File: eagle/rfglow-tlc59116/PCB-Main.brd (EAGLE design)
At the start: 20.1 x 75.9 mm, 14 parts, among them IC1 TLC59116PW, J1 4P-SMD-2.0-90D, J2 2P-2.0-90D-SMD, SW1 MK-12C02 G1.5, SW2 DHT-4235A, X1 87438-06

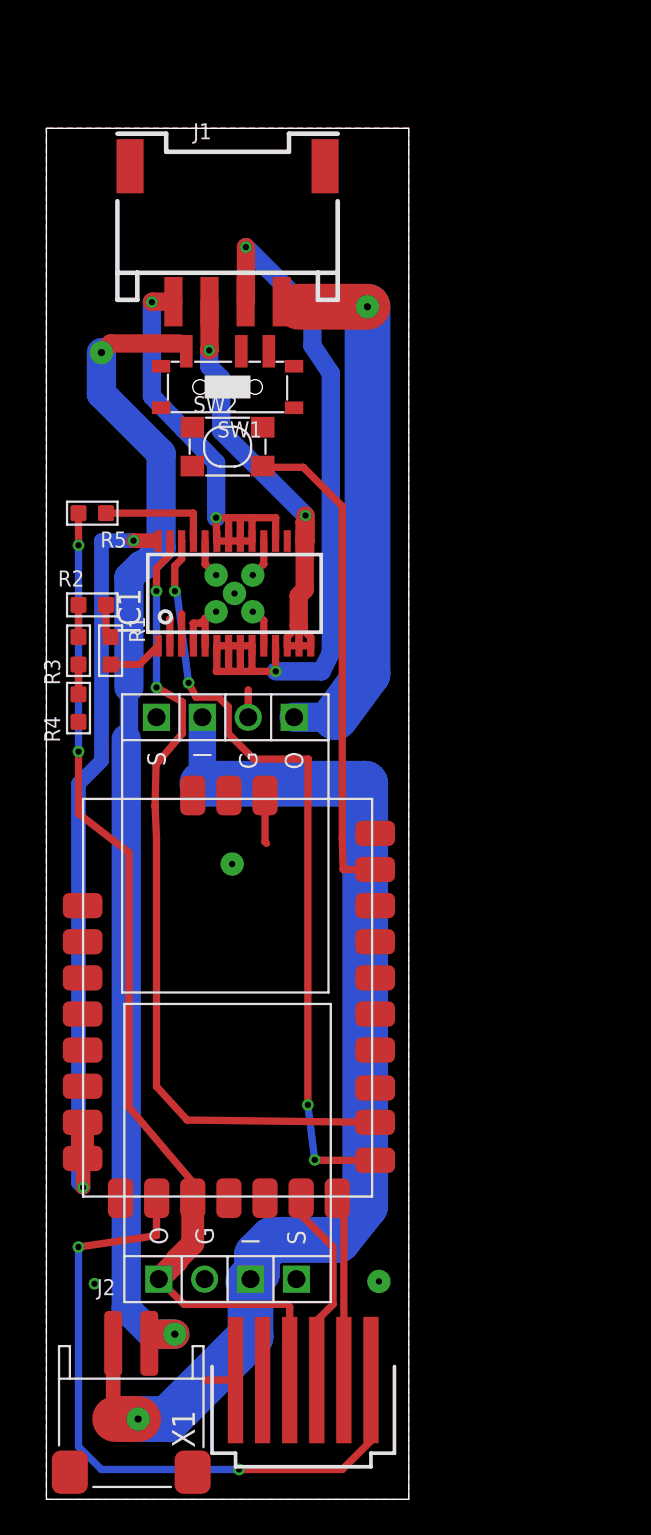
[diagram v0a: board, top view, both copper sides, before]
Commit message: CLeaned up gerbers, fixed serious circuit errors
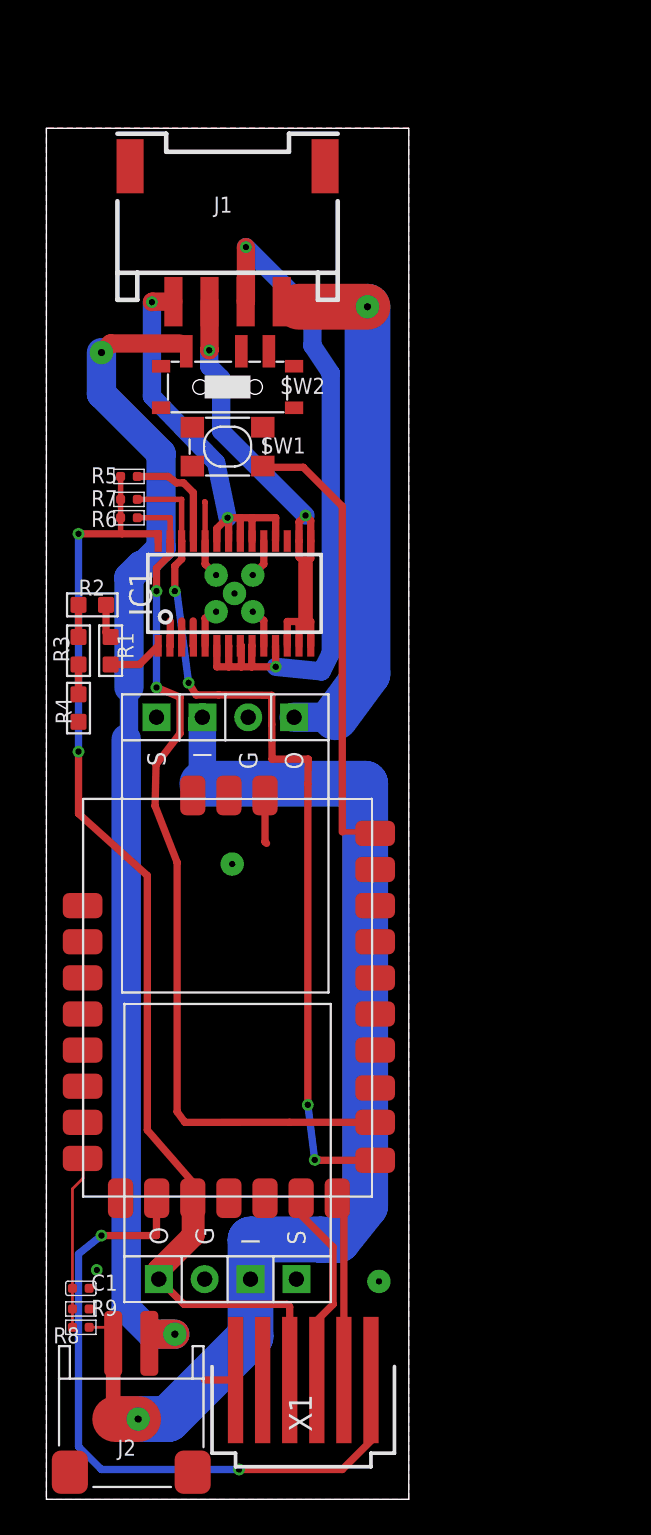
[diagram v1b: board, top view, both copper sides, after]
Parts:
- added C1: 100nf, Seeed-Capacitor:C0402
- added R6, R7: 4.7K, Seeed-Resistor:R0402
- added R8, R9: 10M 1/16W, Seeed-Resistor:R0402
- R5: value 10K -> 10K 1/16W; device Seeed-Resistor:R0603 -> Seeed-Resistor:R0402
- X1: device con-molex:87438-06 -> Components:87438-06
- moved R5 2.87 mm to (-6.86, 51.6)
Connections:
- removed net N$12: IC1.26, U$1.P$18
- removed net N$13: IC1.27, U$1.P$19
- removed net N$8: MOD3.3V.O, R5.1, U$1.P$13, X1.3
- new net I2CSCL: IC1.26, R7.1, U$1.P$18
- new net I2CSDA: IC1.27, R6.1, U$1.P$19
- new net V3.3: IC1.28, MOD3.3V.O, R5.1, R6.2, R7.2, U$1.P$13, X1.3
- net GND: now also C1.1, R9.1
- net N$11: now also U$1.P$27; no longer U$1.P$26
- net N$17: now also C1.2, R8.1, R9.2; no longer IC1.28, U$1.P$9
- net N$5: now also R8.2
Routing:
- net V3.3: track 0.00 -> 64.8 mm, vias 0 -> 2
- net N$8: track 57.8 -> 0.00 mm, vias 2 -> 0
- net I2CSCL: track 0.00 -> 48.9 mm, vias 0 -> 4
- net I2CSDA: track 0.00 -> 48.2 mm, vias 0 -> 2
- net N$13: track 44.8 -> 0.00 mm, vias 2 -> 0
- net N$12: track 43.1 -> 0.00 mm, vias 4 -> 0
- net N$17: track 43.2 -> 9.60 mm, vias 2 -> 0
- net N$14: track 43.4 -> 40.2 mm
- net N$5: track 62.4 -> 65.2 mm
- net N$15: track 26.3 -> 24.0 mm
- net N$11: track 27.2 -> 25.3 mm
- net GND: track 20.6 -> 19.4 mm
- net N$10: track 29.9 -> 29.1 mm

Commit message: Updates to board
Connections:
- new net N$8: U$1.P$11, X1.2
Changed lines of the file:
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@@
 <?xml version="1.0" encoding="utf-8"?>
 <!DOCTYPE eagle SYSTEM "eagle.dtd">
-<eagle version="8.3.0">
+<eagle version="8.3.1">
 <drawing>
 <settings>
@@
 <wire x1="-9.398" y1="13.769" x2="-9.424" y2="13.795" width="0.1524" layer="1"/>
 </signal>
+<signal name="N$8">
+<contactref element="U$1" pad="P$11"/>
+<contactref element="X1" pad="2"/>
+<wire x1="0.544" y1="1.524" x2="-7.324" y2="11.595" width="0" layer="19" extent="1-1"/>
+</signal>
 </signals>

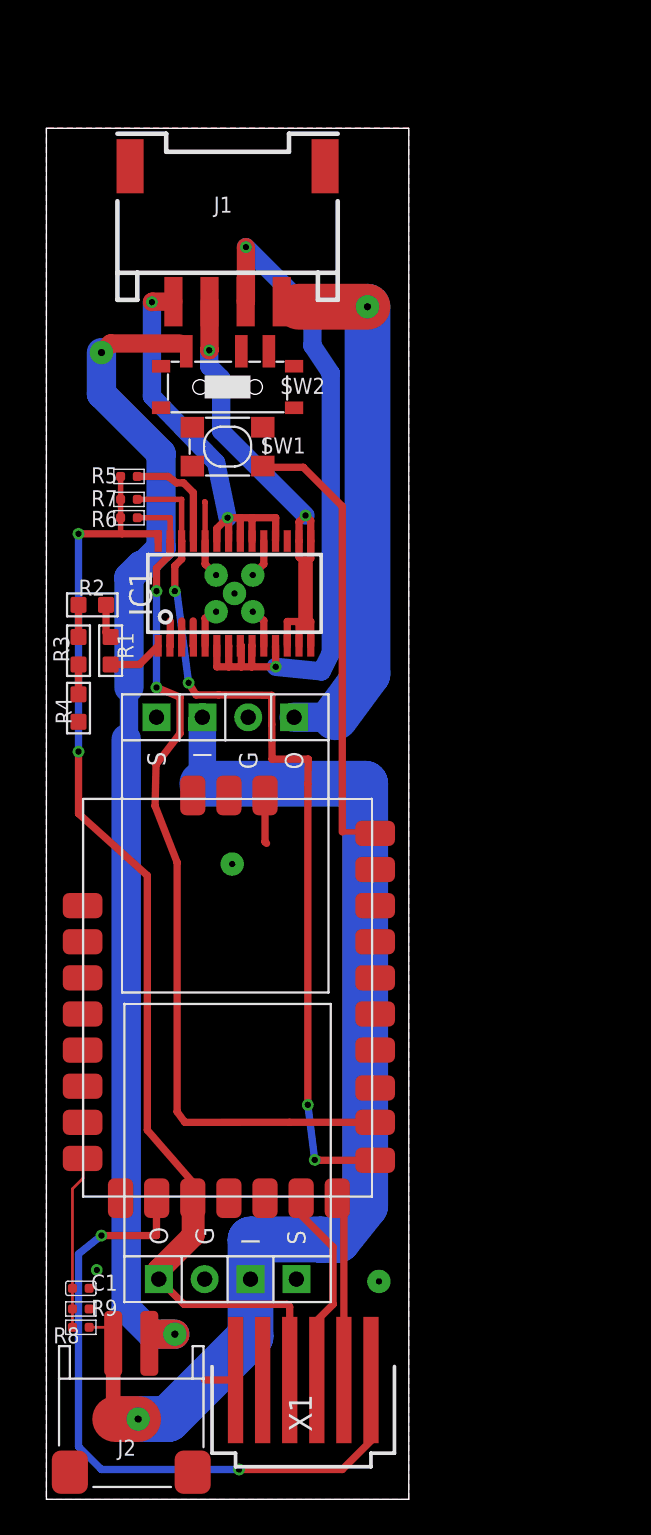
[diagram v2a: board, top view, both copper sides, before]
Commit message: Real PCB for relay board, update handle to reduce submodules and use a u.FL antenna connector.
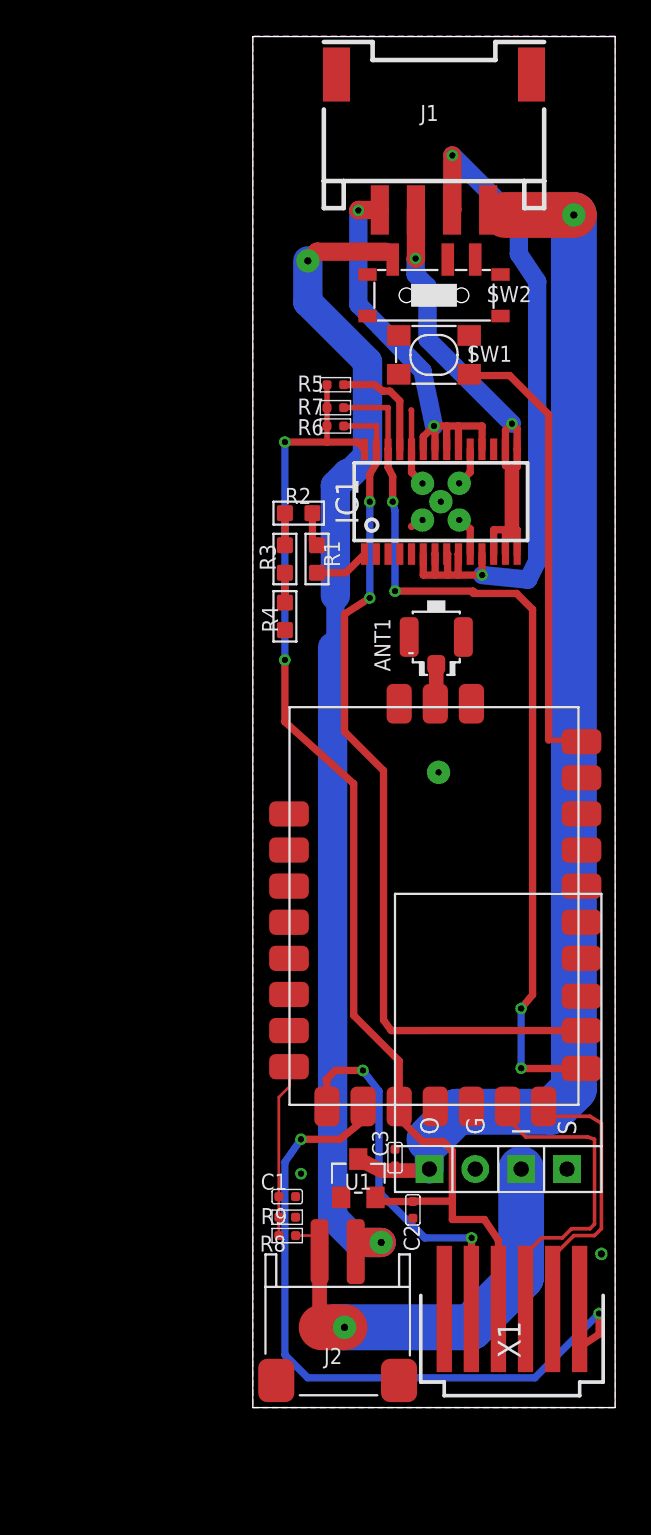
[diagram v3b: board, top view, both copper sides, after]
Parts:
- removed MOD3.3V: POLOLU_S7V8PROD, Components:POLOLU_4P_SIGO
- added ANT1: U-FL, Seeed-Connector:U-FL3P-SMD-2.6X2.6X1.0MM
- added C2, C3: 1uf, Seeed-Capacitor:C0402
- added U1: XC6206P332MR-G-SOT23, Seeed-IC:SOT-23
- moved MOD5V 16.8 mm to (13.6, 22.1), turned to 0 degrees
- moved J1 12.5 mm to (10.0, 66.4)
- moved R1 12.5 mm to (3.56, 47.0)
- moved R3 12.5 mm to (1.78, 47.0)
- moved R5 12.5 mm to (4.57, 56.6)
- moved C1 12.5 mm to (1.91, 11.7)
- moved IC1 12.5 mm to (10.4, 50.2)
- moved J2 12.5 mm to (4.70, 3.68)
- moved R2 12.5 mm to (2.54, 49.5)
- moved R4 12.5 mm to (1.78, 43.8)
- moved R6 12.5 mm to (4.57, 54.4)
- moved R7 12.5 mm to (4.57, 55.4)
- moved R8 12.5 mm to (1.91, 9.53)
- moved R9 12.5 mm to (1.91, 10.5)
- moved SW1 12.5 mm to (10.0, 61.6)
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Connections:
- net N$6 renamed SW-GND
- removed net N$5: J2.+, MOD3.3V.I, MOD5V.I, R8.2
- new net V4.5: C3.2, J1.4, MOD5V.O, U1.3
- new net VBAT: J2.+, MOD5V.I, R8.2
- net GND: now also ANT1.GND1, ANT1.GND2, C2.1, C3.1, U1.1; no longer MOD3.3V.G
- net N$1: now also ANT1.D, U$1.P$31; no longer J1.4, MOD5V.O
- net V3.3: now also C2.2, U1.2; no longer MOD3.3V.O
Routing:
- net V4.5: track 0.00 -> 68.4 mm, vias 0 -> 1
- net N$5: track 65.2 -> 0.00 mm, vias 1 -> 0
- net N$1: track 30.5 -> 2.20 mm, vias 1 -> 0
- net VBAT: track 0.00 -> 25.3 mm, vias 0 -> 1
- net N$8: track 0.00 -> 20.9 mm, vias 0 -> 2
- net N$18: track 10.2 -> 22.5 mm
- net GND: track 19.4 -> 9.35 mm
- net N$16: track 11.3 -> 18.7 mm
- net N$19: track 38.2 -> 43.1 mm
- net V3.3: track 64.8 -> 68.8 mm
- net I2CSCL: track 48.9 -> 49.8 mm

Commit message: Clean up schematic
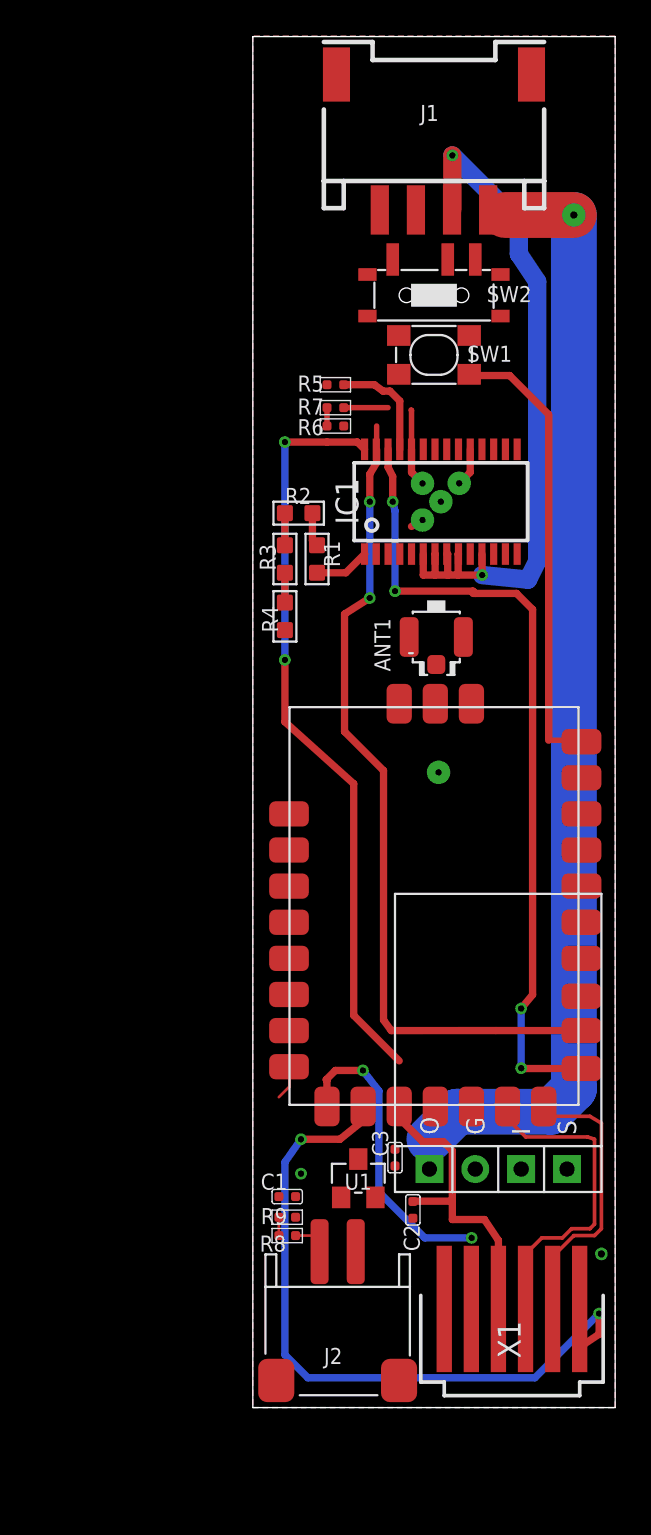
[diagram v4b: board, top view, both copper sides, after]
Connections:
- net N$1 renamed ANT
- net N$10 renamed GREEN-
- net N$11 renamed BUTTON
- net N$14 renamed RED-
- net N$15 renamed BLUE-
- net N$16 renamed TXD
- net N$18 renamed RXD
- net N$19 renamed RST
- net N$8 renamed AREF
- net SW-GND renamed BAT-
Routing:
- net BAT-: track 65.2 -> 0.00 mm, vias 2 -> 0
- net GREEN-: track 28.7 -> 0.00 mm, vias 2 -> 0
- net BLUE-: track 24.0 -> 0.00 mm, vias 2 -> 0
- net VBAT: track 25.3 -> 1.33 mm, vias 1 -> 0
- net V3.3: track 68.8 -> 61.9 mm
- net N$17: track 9.60 -> 2.96 mm
- net V4.5: track 68.4 -> 62.4 mm
- net AREF: track 20.9 -> 17.0 mm
- net TXD: track 18.7 -> 15.6 mm
- net RXD: track 22.5 -> 19.6 mm
- net I2CSCL: track 49.8 -> 47.5 mm
- net ANT: track 2.20 -> 0.00 mm
- net GND: track 9.35 -> 7.17 mm, vias 8 -> 7
- net I2CSDA: track 48.1 -> 46.3 mm
- net RST: track 43.1 -> 42.0 mm
